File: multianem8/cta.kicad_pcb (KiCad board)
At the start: 2 copper layers, 268 x 157.5 mm, 285 parts, among them Q1 TIP41, Q10 TIP41, Q11 TIP41, Q12 TIP41, Q13 TIP41, Q14 TIP41, Q15 TIP41, Q16 TIP41, Q2 TIP41, Q3 TIP41, Q4 TIP41, Q5 TIP41, Q6 TIP41, Q7 TIP41, Q8 TIP41, Q9 TIP41, U1 LM324, U10 LM324, U11 LM324, U12 LM324, U13 LM324, U14 LM324, U15 LM324, U16 LM324, U2 LM324, U3 LM324, U4 LM324, U5 LM324, U6 LM324, U7 LM324, U8 LM324, U9 LM324

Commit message: Created the multiname8 board
I recycled the multinam16 board and the numbering of each anemometer's component is 1-4 and 9-12. I might (might...) change the numbering 9-12 to 5-8. The output is also inverted inthe flat cable coming out of the board.
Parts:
- removed CI13, CI14, CI15, CI16, CI5, CI6, CI7, CI8: 100n, Capacitor_THT:C_Rect_L7.2mm_W3.5mm_P5.00mm_FKS2_FKP2_MKS2_MKP2
- removed Cf13, Cf14, Cf15, Cf16, Cf5, Cf6, Cf7, Cf8: 1u, Capacitor_THT:CP_Radial_D5.0mm_P2.50mm
- removed Cua13, Cua14, Cua15, Cua16, Cua5, Cua6, Cua7, Cua8, Cub13, Cub14, Cub15, Cub16, Cub5, Cub6, Cub7, Cub8: 100n, Capacitor_THT:C_Disc_D5.0mm_W2.5mm_P2.50mm
- removed Don13, Don14, Don15, Don16, Don5, Don6, Don7, Don8: 1N4148, Diode_THT:D_DO-35_SOD27_P7.62mm_Horizontal
- removed JOUT2: Conn_01x08, Connector_PinHeader_2.54mm:PinHeader_1x08_P2.54mm_Vertical
- removed Jw13, Jw14, Jw15, Jw16, Jw5, Jw6, Jw7, Jw8: Conn_01x02, Connector_PinHeader_2.54mm:PinHeader_1x02_P2.54mm_Vertical
- removed Q13, Q14, Q15, Q16, Q5, Q6, Q7, Q8: TIP41, Package_TO_SOT_THT:TO-220-3_Vertical
- removed the REF** at (275.6, 167.6)
- removed the REF** at (17.8, 167.6)
- removed the REF** at (17.8, 20.3)
- removed the REF** at (275.6, 20.3)
- removed Ra13, Ra14, Ra15, Ra16, Ra5, Ra6, Ra7, Ra8: 100, Resistor_THT:R_Axial_DIN0207_L6.3mm_D2.5mm_P10.16mm_Horizontal
- removed Rb13, Rb14, Rb15, Rb16, Rb5, Rb6, Rb7, Rb8: 10, Resistor_THT:R_Axial_DIN0414_L11.9mm_D4.5mm_P15.24mm_Horizontal
- removed Rc13, Rc14, Rc15, Rc16, Rc5, Rc6, Rc7, Rc8: 1k, Resistor_THT:R_Axial_DIN0207_L6.3mm_D2.5mm_P10.16mm_Horizontal
- removed Rda13, Rda14, Rda15, Rda16, Rda5, Rda6, Rda7, Rda8: 100k, Resistor_THT:R_Axial_DIN0207_L6.3mm_D2.5mm_P10.16mm_Horizontal
- removed Rdb13, Rdb14, Rdb15, Rdb16, Rdb5, Rdb6, Rdb7, Rdb8: 20k, Resistor_THT:R_Axial_DIN0207_L6.3mm_D2.5mm_P10.16mm_Horizontal
- removed Rf13, Rf14, Rf15, Rf16, Rf5, Rf6, Rf7, Rf8, Rua13, Rua14, Rua15, Rua16, Rua5, Rua6, Rua7, Rua8, Rub13, Rub14, Rub15, Rub16, Rub5, Rub6, Rub7, Rub8: 10k, Resistor_THT:R_Axial_DIN0207_L6.3mm_D2.5mm_P10.16mm_Horizontal
- removed Rt13, Rt14, Rt15, Rt16, Rt5, Rt6, Rt7, Rt8: 2k, Resistor_THT:R_Axial_DIN0207_L6.3mm_D2.5mm_P10.16mm_Horizontal
- removed U13, U14, U15, U16, U5, U6, U7, U8: LM324, Package_DIP:DIP-14_W7.62mm_LongPads
- added REF**: MountingHole_3.5mm_Pad, MountingHole:MountingHole_3.5mm_Pad, F.Cu at (210.8, 19.1)
- added REF**: MountingHole_3.5mm_Pad, MountingHole:MountingHole_3.5mm_Pad, F.Cu at (210.8, 157.5)
- added REF**: MountingHole_3.5mm_Pad, MountingHole:MountingHole_3.5mm_Pad, F.Cu at (55.9, 157.5)
- added REF**: MountingHole_3.5mm_Pad, MountingHole:MountingHole_3.5mm_Pad, F.Cu at (55.9, 19.1)
- JOUT1: value Conn_01x08 -> Conn_01x09; footprint Connector_PinHeader_2.54mm:PinHeader_1x08_P2.54mm_Vertical -> Connector_PinHeader_2.54mm:PinHeader_1x09_P2.54mm_Vertical
- moved Coo1 78.8 mm to (198.1, 71.1)
- moved Roo2 78.8 mm to (198.1, 85.1)
- moved Roo3 78.8 mm to (194.3, 85.1)
- moved Roo1 73.7 mm to (194.3, 66.0), turned to 90 degrees
- moved Qon1 72.3 mm to (190.5, 66.0), turned to 180 degrees
- moved JVIN1 67.0 mm to (207.0, 76.2)
- moved D1 66.5 mm to (189.2, 72.4), turned to 270 degrees
- moved Q12 36.1 mm to (181.6, 130.8)
- moved Cua10 36.1 mm to (99.1, 115.6)
- moved Cua12 36.1 mm to (160.0, 115.6)
- moved Cub11 36.1 mm to (146.1, 109.2)
- moved Cub9 36.1 mm to (85.1, 109.2)
- moved Don11 36.1 mm to (149.9, 146.1)
- moved Q10 36.1 mm to (120.7, 130.8)
- moved Ra10 36.1 mm to (111.8, 130.8)
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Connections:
- JOUT1 pad 5: /VO5 -> /VO12
- JOUT1 pad 6: /VO6 -> /VO11
- JOUT1 pad 7: /VO7 -> /VO10
- JOUT1 pad 8: /VO8 -> /VO9
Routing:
- net GND: track 2639.4 -> 1389.4 mm, vias 0 -> 7
- net VCC: track 1567.8 -> 765.8 mm, vias 32 -> 16
- net /VON1: track 1074.5 -> 390.7 mm, vias 3 -> 0
- net VEE: track 843.2 -> 402.8 mm, vias 32 -> 16
- net /VO16: track 253.9 -> 0.00 mm
- net /VO8: track 247.8 -> 0.00 mm
- net /VO15: track 221.3 -> 0.00 mm
- net /VO7: track 217.4 -> 0.00 mm
- net /VO14: track 188.6 -> 0.00 mm
- net /VO6: track 186.9 -> 0.00 mm
- net /VO13: track 156.6 -> 0.00 mm
- net /VO5: track 156.4 -> 0.00 mm
- net Net-(Jw15-Pad1): track 55.3 -> 0.00 mm
- net Net-(Jw8-Pad1): track 55.3 -> 0.00 mm
- net Net-(Jw5-Pad1): track 55.3 -> 0.00 mm
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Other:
- board size 268 x 157.5 mm -> 165.1 x 148.6 mm

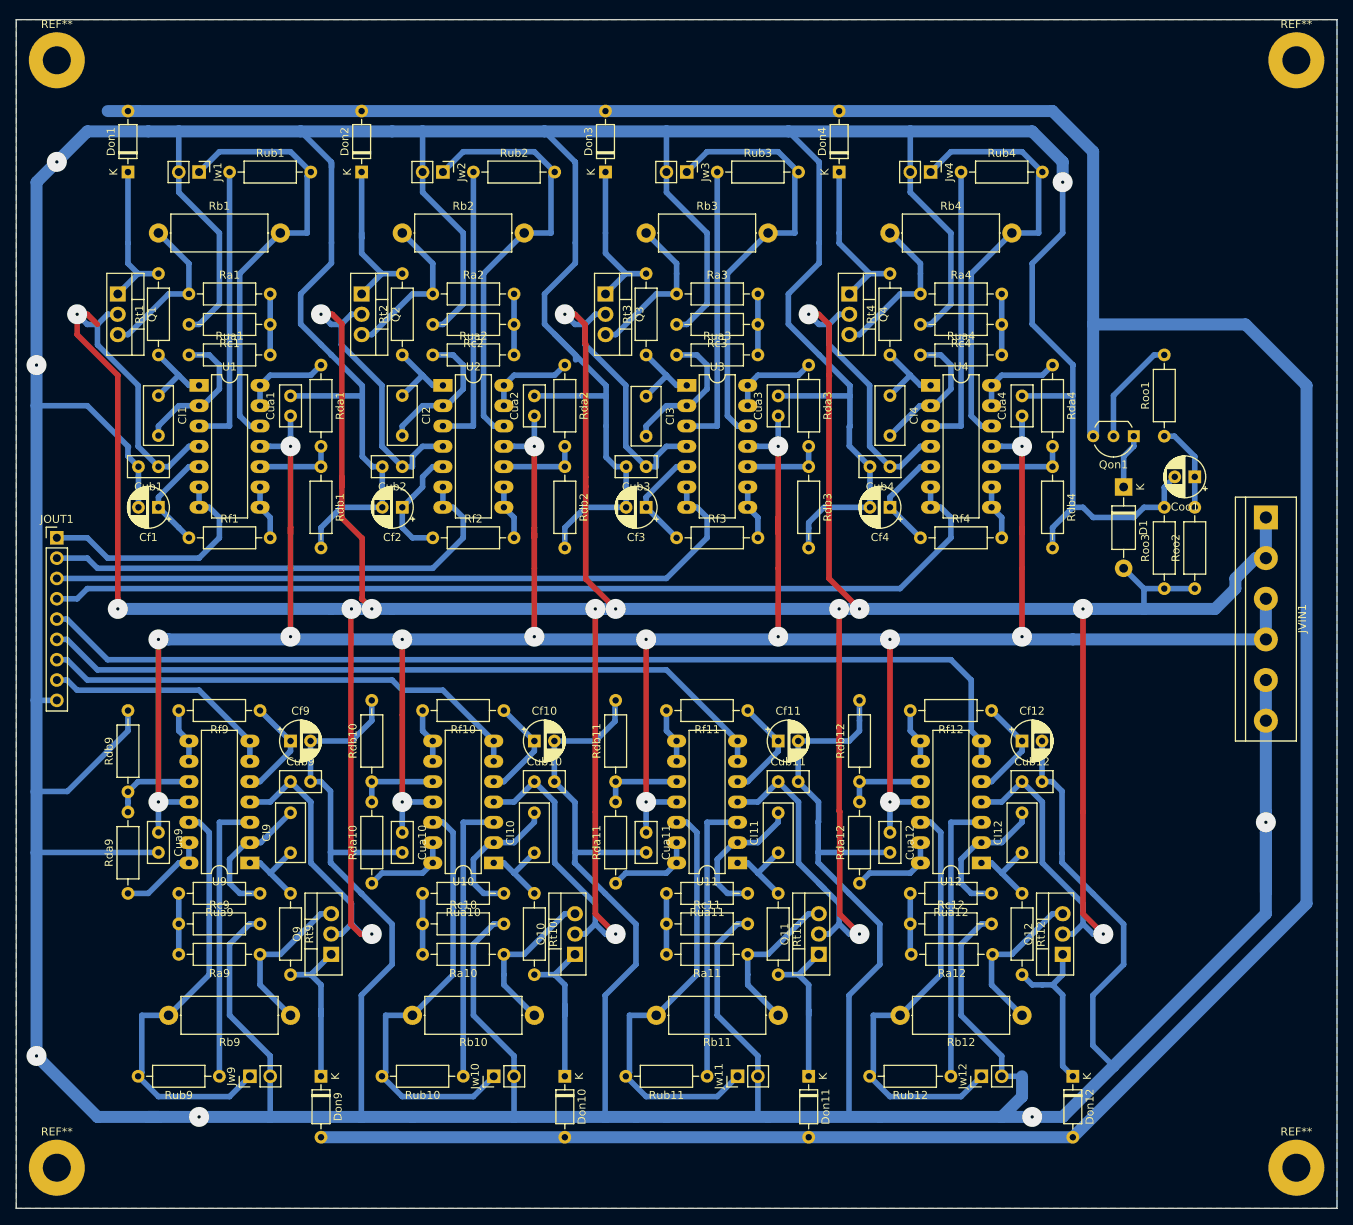
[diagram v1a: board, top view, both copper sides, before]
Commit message: Created gerber files for fabrication
I will try to build the board on some fab.
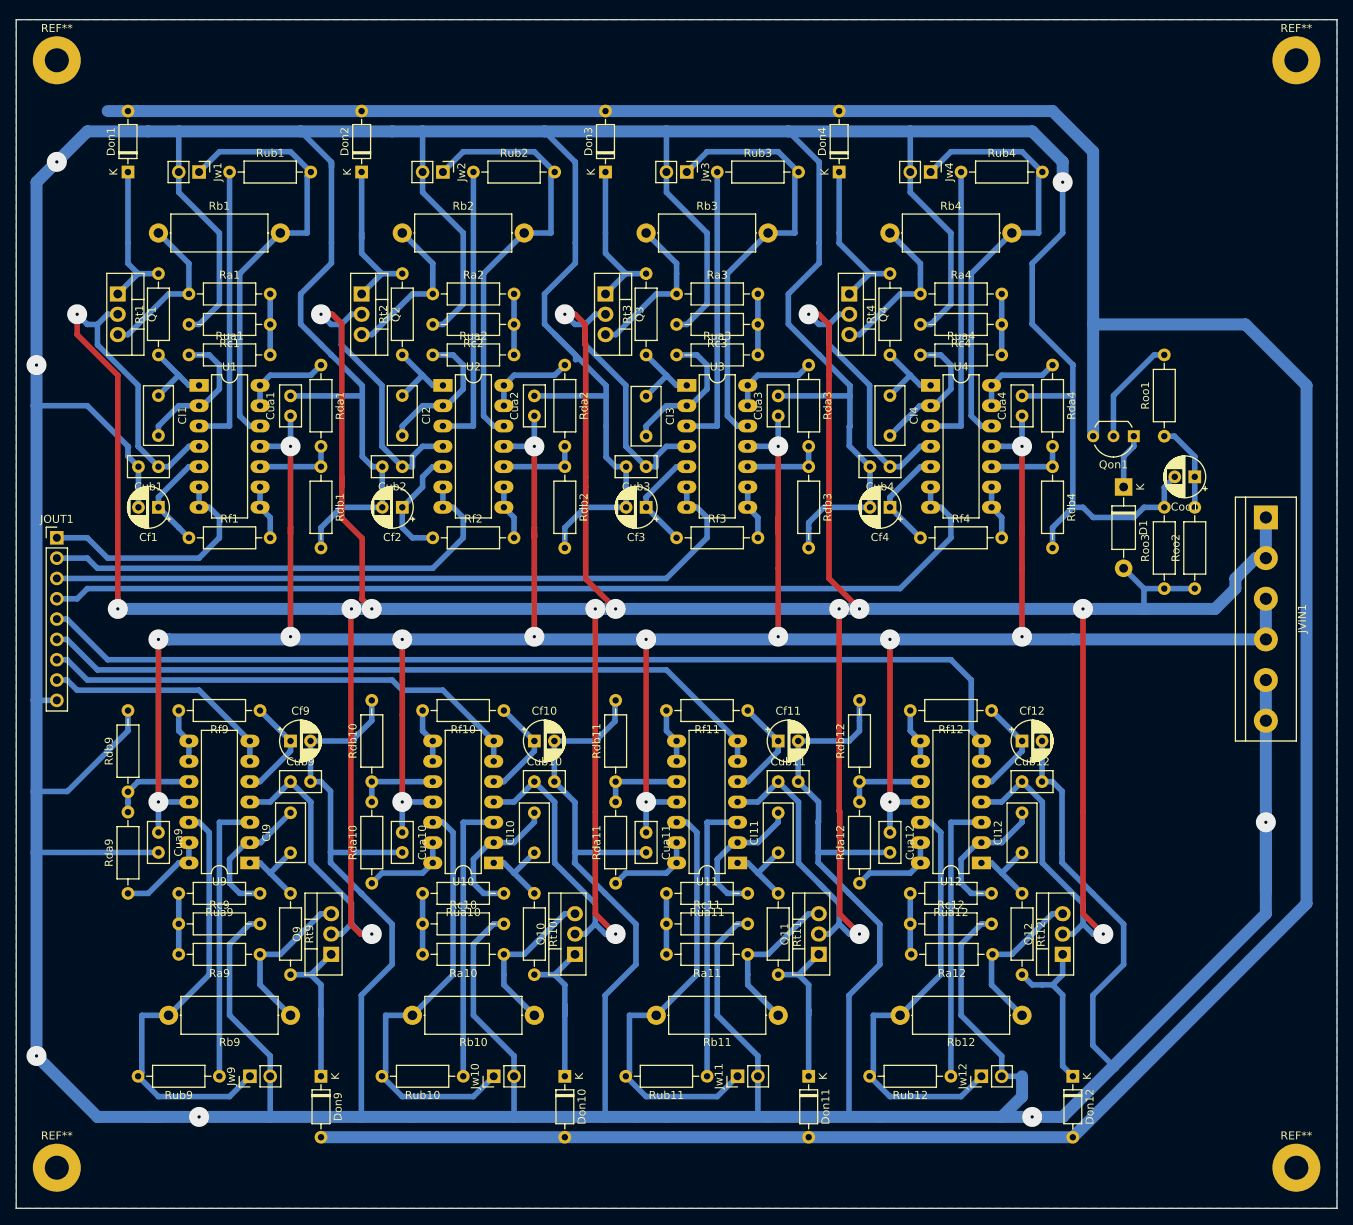
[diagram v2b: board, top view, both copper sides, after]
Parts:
- removed the REF** at (210.8, 19.1)
- removed the REF** at (210.8, 157.5)
- removed the REF** at (55.9, 157.5)
- removed the REF** at (55.9, 19.1)
- added REF**: MountingHole_3mm_Pad, MountingHole:MountingHole_3mm_Pad, F.Cu at (210.8, 19.1)
- added REF**: MountingHole_3mm_Pad, MountingHole:MountingHole_3mm_Pad, F.Cu at (210.8, 157.5)
- added REF**: MountingHole_3mm_Pad, MountingHole:MountingHole_3mm_Pad, F.Cu at (55.9, 157.5)
- added REF**: MountingHole_3mm_Pad, MountingHole:MountingHole_3mm_Pad, F.Cu at (55.9, 19.1)
- Roo1: value 10 -> 100
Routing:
- net VCC: track 765.8 -> 762.8 mm
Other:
- rule pad_to_mask_clearance: 0.05 -> 0
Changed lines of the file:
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@@
     (thickness 1.6)
     (drawings 4)
-    (tracks 1007)
+    (tracks 1005)
     (zones 0)
     (modules 148)
@@
     (32 B.Adhes user hide)
     (33 F.Adhes user hide)
-    (34 B.Paste user hide)
-    (35 F.Paste user hide)
-    (36 B.SilkS user hide)
+    (34 B.Paste user)
+    (35 F.Paste user)
+    (36 B.SilkS user)
     (37 F.SilkS user)
-    (38 B.Mask user hide)
-    (39 F.Mask user hide)
+    (38 B.Mask user)
+    (39 F.Mask user)
     (40 Dwgs.User user hide)
     (41 Cmts.User user hide)
@@
     (47 F.CrtYd user hide)
     (48 B.Fab user hide)
-    (49 F.Fab user)
+    (49 F.Fab user hide)
   )
   (setup
-    (last_trace_width 1.5)
+    (last_trace_width 0.25)
     (user_trace_width 0.5)
     (user_trace_width 0.7)
@@
     (pad_size 1.524 1.524)
     (pad_drill 0.762)
-    (pad_to_mask_clearance 0.05)
+    (pad_to_mask_clearance 0)
     (aux_axis_origin 0 0)
     (visible_elements FFFFFF7F)
     (pcbplotparams
       (layerselection 0x010fc_ffffffff)
-      (usegerberextensions false)
+      (usegerberextensions true)
       (usegerberattributes true)
-      (usegerberadvancedattributes true)
-      (creategerberjobfile true)
+      (usegerberadvancedattributes false)
+      (creategerberjobfile false)
       (excludeedgelayer true)
       (linewidth 0.100000)
@@
       (psa4output false)
       (plotreference true)
-      (plotvalue true)
+      (plotvalue false)
       (plotinvisibletext false)
       (padsonsilk false)
-      (subtractmaskfromsilk false)
+      (subtractmaskfromsilk true)
       (outputformat 1)
       (mirror false)
-      (drillshape 1)
+      (drillshape 0)
       (scaleselection 1)
-      (outputdirectory ""))
+      (outputdirectory "Gerber"))
   )
   (net 0 "")
@@
     (add_net VEE)
   )
-  (module MountingHole:MountingHole_3.5mm_Pad (layer F.Cu)
+  (module MountingHole:MountingHole_3mm_Pad (layer F.Cu)
     (at 210.82 19.05)
-    (descr "Mounting Hole 3.5mm")
-    (tags "mounting hole 3.5mm")
+    (descr "Mounting Hole 3mm")
+    (tags "mounting hole 3mm")
     (attr virtual)
-    (fp_text reference REF** (at 0 -4.5) (layer F.SilkS)
+    (fp_text reference REF** (at 0 -4) (layer F.SilkS)
       (effects (font (size 1 1) (thickness 0.15)))
     )
-    (fp_text value MountingHole_3.5mm_Pad (at -6.35 6.35) (layer F.Fab)
+    (fp_text value MountingHole_3mm_Pad (at -7.62 6.35) (layer F.Fab)
       (effects (font (size 1 1) (thickness 0.15)))
     )
+    (fp_circle (center 0 0) (end 3.25 0) (layer F.CrtYd) (width 0.05))
+    (fp_circle (center 0 0) (end 3 0) (layer Cmts.User) (width 0.15))
     (fp_text user %R (at 0.3 0) (layer F.Fab)
       (effects (font (size 1 1) (thickness 0.15)))
     )
-    (fp_circle (center 0 0) (end 3.5 0) (layer Cmts.User) (width 0.15))
-    (fp_circle (center 0 0) (end 3.75 0) (layer F.CrtYd) (width 0.05))
-    (pad 1 thru_hole circle (at 0 0) (size 7 7) (drill 3.5) (layers *.Cu *.Mask))
+    (pad 1 thru_hole circle (at 0 0) (size 6 6) (drill 3) (layers *.Cu *.Mask))
   )
-  (module MountingHole:MountingHole_3.5mm_Pad (layer F.Cu)
+  (module MountingHole:MountingHole_3mm_Pad (layer F.Cu)
     (at 210.82 157.48)
-    (descr "Mounting Hole 3.5mm")
-    (tags "mounting hole 3.5mm")
+    (descr "Mounting Hole 3mm")
+    (tags "mounting hole 3mm")
     (attr virtual)
-    (fp_text reference REF** (at 0 -4.5) (layer F.SilkS)
+    (fp_text reference REF** (at 0 -4) (layer F.SilkS)
       (effects (font (size 1 1) (thickness 0.15)))
     )
-    (fp_text value MountingHole_3.5mm_Pad (at -12.7 3.81) (layer F.Fab)
+    (fp_text value MountingHole_3mm_Pad (at -12.7 2.54) (layer F.Fab)
       (effects (font (size 1 1) (thickness 0.15)))
     )
+    (fp_circle (center 0 0) (end 3.25 0) (layer F.CrtYd) (width 0.05))
+    (fp_circle (center 0 0) (end 3 0) (layer Cmts.User) (width 0.15))
     (fp_text user %R (at 0.3 0) (layer F.Fab)
       (effects (font (size 1 1) (thickness 0.15)))
     )
-    (fp_circle (center 0 0) (end 3.5 0) (layer Cmts.User) (width 0.15))
-    (fp_circle (center 0 0) (end 3.75 0) (layer F.CrtYd) (width 0.05))
-    (pad 1 thru_hole circle (at 0 0) (size 7 7) (drill 3.5) (layers *.Cu *.Mask))
+    (pad 1 thru_hole circle (at 0 0) (size 6 6) (drill 3) (layers *.Cu *.Mask))
   )
-  (module MountingHole:MountingHole_3.5mm_Pad (layer F.Cu)
+  (module MountingHole:MountingHole_3mm_Pad (layer F.Cu)
     (at 55.88 157.48)
-    (descr "Mounting Hole 3.5mm")
-    (tags "mounting hole 3.5mm")
+    (descr "Mounting Hole 3mm")
+    (tags "mounting hole 3mm")
     (attr virtual)
-    (fp_text reference REF** (at 0 -4.5) (layer F.SilkS)
+    (fp_text reference REF** (at 0 -4) (layer F.SilkS)
       (effects (font (size 1 1) (thickness 0.15)))
     )
-    (fp_text value MountingHole_3.5mm_Pad (at 15.24 2.54) (layer F.Fab)
+    (fp_text value MountingHole_3mm_Pad (at 12.7 2.54) (layer F.Fab)
       (effects (font (size 1 1) (thickness 0.15)))
     )
+    (fp_circle (center 0 0) (end 3.25 0) (layer F.CrtYd) (width 0.05))
+    (fp_circle (center 0 0) (end 3 0) (layer Cmts.User) (width 0.15))
     (fp_text user %R (at 0.3 0) (layer F.Fab)
       (effects (font (size 1 1) (thickness 0.15)))
     )
-    (fp_circle (center 0 0) (end 3.5 0) (layer Cmts.User) (width 0.15))
-    (fp_circle (center 0 0) (end 3.75 0) (layer F.CrtYd) (width 0.05))
-    (pad 1 thru_hole circle (at 0 0) (size 7 7) (drill 3.5) (layers *.Cu *.Mask))
+    (pad 1 thru_hole circle (at 0 0) (size 6 6) (drill 3) (layers *.Cu *.Mask))
   )
-  (module MountingHole:MountingHole_3.5mm_Pad (layer F.Cu)
+  (module MountingHole:MountingHole_3mm_Pad (layer F.Cu)
     (at 55.88 19.05)
-    (descr "Mounting Hole 3.5mm")
-    (tags "mounting hole 3.5mm")
+    (descr "Mounting Hole 3mm")
+    (tags "mounting hole 3mm")
     (attr virtual)
-    (fp_text reference REF** (at 0 -4.5) (layer F.SilkS)
+    (fp_text reference REF** (at 0 -4) (layer F.SilkS)
       (effects (font (size 1 1) (thickness 0.15)))
     )
-    (fp_text value MountingHole_3.5mm_Pad (at 15.24 1.27) (layer F.Fab)
+    (fp_text value MountingHole_3mm_Pad (at 13.97 2.54) (layer F.Fab)
       (effects (font (size 1 1) (thickness 0.15)))
     )
+    (fp_circle (center 0 0) (end 3.25 0) (layer F.CrtYd) (width 0.05))
+    (fp_circle (center 0 0) (end 3 0) (layer Cmts.User) (width 0.15))
     (fp_text user %R (at 0.3 0) (layer F.Fab)
       (effects (font (size 1 1) (thickness 0.15)))
     )
-    (fp_circle (center 0 0) (end 3.5 0) (layer Cmts.User) (width 0.15))
-    (fp_circle (center 0 0) (end 3.75 0) (layer F.CrtYd) (width 0.05))
-    (pad 1 thru_hole circle (at 0 0) (size 7 7) (drill 3.5) (layers *.Cu *.Mask))
+    (pad 1 thru_hole circle (at 0 0) (size 6 6) (drill 3) (layers *.Cu *.Mask))
   )
   (module TerminalBlock:TerminalBlock_bornier-6_P5.08mm (layer F.Cu)
@@
       (effects (font (size 1 1) (thickness 0.15)))
     )
-    (fp_text user %R (at 12.7 0 90) (layer F.Fab)
-      (effects (font (size 1 1) (thickness 0.15)))
-    )
     (fp_line (start -2.5 2.55) (end 27.9 2.55) (layer F.Fab) (width 0.1))
     (fp_line (start -2.5 -3.75) (end -2.5 3.75) (layer F.Fab) (width 0.1))
@@
     (fp_line (start 28.15 4) (end 28.15 -4) (layer F.CrtYd) (width 0.05))
     (fp_line (start 28.15 4) (end -2.75 4) (layer F.CrtYd) (width 0.05))
+    (fp_text user %R (at 12.7 0 90) (layer F.Fab)
+      (effects (font (size 1 1) (thickness 0.15)))
+    )
     (pad 6 thru_hole circle (at 25.4 0 270) (size 3 3) (drill 1.52) (layers *.Cu *.Mask)
       (net 2 GND))
@@
       (effects (font (size 1 1) (thickness 0.15)))
     )
-    (fp_text user %R (at 3.81 7.62) (layer F.Fab)
-      (effects (font (size 1 1) (thickness 0.15)))
-    )
-    (fp_arc (start 3.81 -1.33) (end 2.81 -1.33) (angle -180) (layer F.SilkS) (width 0.12))
     (fp_line (start 1.635 -1.27) (end 6.985 -1.27) (layer F.Fab) (width 0.1))
     (fp_line (start 6.985 -1.27) (end 6.985 16.51) (layer F.Fab) (width 0.1))
@@
     (fp_line (start 9.1 16.8) (end 9.1 -1.55) (layer F.CrtYd) (width 0.05))
     (fp_line (start 9.1 -1.55) (end -1.45 -1.55) (layer F.CrtYd) (width 0.05))
+    (fp_text user %R (at 3.81 7.62) (layer F.Fab)
+      (effects (font (size 1 1) (thickness 0.15)))
+    )
+    (fp_arc (start 3.81 -1.33) (end 2.81 -1.33) (angle -180) (layer F.SilkS) (width 0.12))
     (pad 14 thru_hole oval (at 7.62 0 180) (size 2.4 1.6) (drill 0.8) (layers *.Cu *.Mask)
       (net 44 "Net-(Rda9-Pad1)"))
@@
       (effects (font (size 1 1) (thickness 0.15)))
     )
-    (fp_text user %R (at 0 10.16 90) (layer F.Fab)
-      (effects (font (size 1 1) (thickness 0.15)))
-    )
     (fp_line (start -0.635 -1.27) (end 1.27 -1.27) (layer F.Fab) (width 0.1))
     (fp_line (start 1.27 -1.27) (end 1.27 21.59) (layer F.Fab) (width 0.1))
@@
     (fp_line (start 1.8 22.1) (end 1.8 -1.8) (layer F.CrtYd) (width 0.05))
     (fp_line (start 1.8 -1.8) (end -1.8 -1.8) (layer F.CrtYd) (width 0.05))
+    (fp_text user %R (at 0 10.16 90) (layer F.Fab)
+      (effects (font (size 1 1) (thickness 0.15)))
+    )
     (pad 9 thru_hole oval (at 0 20.32) (size 1.7 1.7) (drill 1) (layers *.Cu *.Mask)
       (net 2 GND))
@@
       (effects (font (size 1 1) (thickness 0.15)))
     )
-    (fp_text value 10 (at 5.08 2.37 90) (layer F.Fab)
+    (fp_text value 100 (at 5.08 2.37 90) (layer F.Fab)
       (effects (font (size 1 1) (thickness 0.15)))
     )
@@
   (via (at 58.42 50.8) (size 2.5) (drill 0.4) (layers F.Cu B.Cu) (net 3))
   (segment (start 59.69 52.07) (end 58.42 50.8) (width 0.7) (layer B.Cu) (net 3))
-  (segment (start 58.42 50.8) (end 59.69 50.8) (width 0.7) (layer F.Cu) (net 3))
-  (segment (start 59.69 50.8) (end 60.96 52.07) (width 0.7) (layer F.Cu) (net 3))
   (via (at 63.5 87.63) (size 2.5) (drill 0.4) (layers F.Cu B.Cu) (net 3))
   (segment (start 94.05 86.29) (end 93.98 86.36) (width 0.7) (layer F.Cu) (net 3))
